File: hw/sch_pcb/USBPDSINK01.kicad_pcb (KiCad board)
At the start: 2 copper layers, 40.1 x 50.3 mm, 51 parts, among them J1 USBC_USB4105-GF-A, J2 HEADER_2x05_PARALLEL, J3 HEADER_2x04_PARALLEL, J4 HEADER_2x03_PARALLEL, J5 HEADER_2x01, J6 HEADER_2x07_PARALLEL, M1 HOLE, M2 HOLE, M3 HOLE, M4 HOLE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

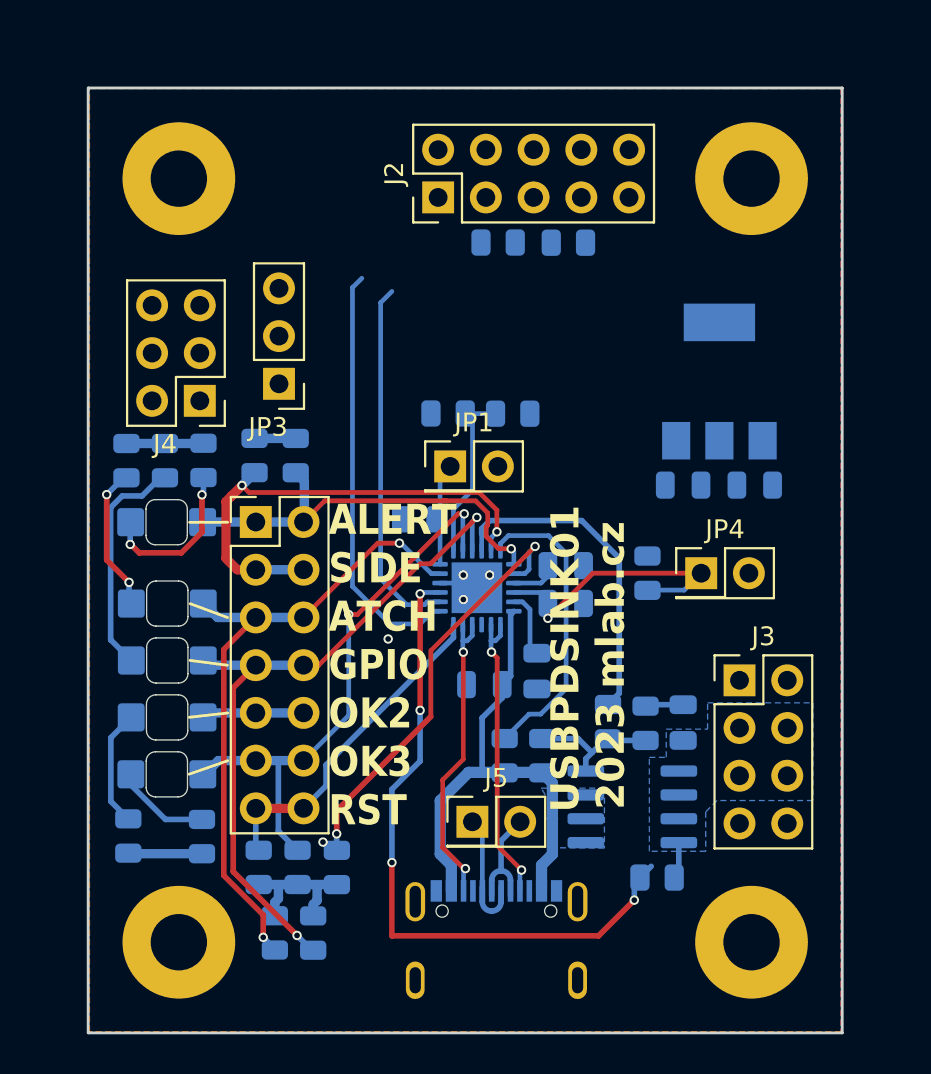
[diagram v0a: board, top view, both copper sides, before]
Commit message: update improvements in schematics and layout
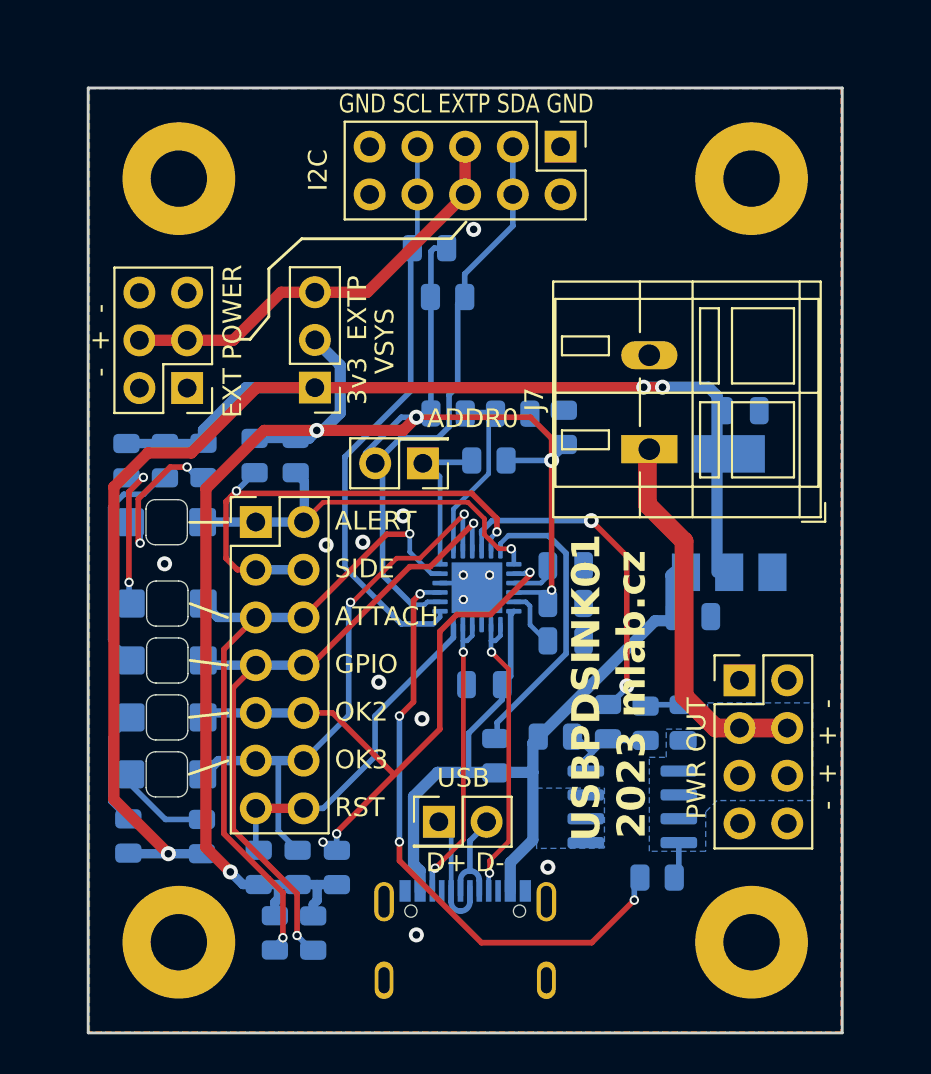
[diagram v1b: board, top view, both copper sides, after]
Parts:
- removed JP4: Jumper_2_Open, Connector_PinHeader_2.54mm:PinHeader_2x01_P2.54mm_Vertical
- added J7: WAGO, TerminalBlock_WAGO:TerminalBlock_WAGO_236-102_1x02_P5.00mm_45Degree, F.Cu at (158.3, 99.1)
- moved R22 8.95 mm to (153.8, 97.9)
- moved R14 7.40 mm to (146.6, 88.4), turned to 180 degrees
- moved J2 7.05 mm to (153.6, 83.0), turned to -90 degrees
- moved C6 7.02 mm to (160.6, 108.0)
- moved U2 7.02 mm to (162.6, 102.5)
- moved R1 4.87 mm to (149.8, 99.7), turned to 180 degrees
- moved C5 4.02 mm to (163.2, 97.0)
- moved R13 3.96 mm to (147.6, 91.0), turned to 0 degrees
- moved C1 2.22 mm to (153.8, 109.3), turned to 0 degrees
- moved JP3 1.92 mm to (140.5, 95.8)
- moved J5 1.78 mm to (147.1, 118.9)
- moved J1 1.66 mm to (148.5, 127.3)
- moved JP1 1.46 mm to (146.2, 99.8), turned to 180 degrees
- moved R10 1.23 mm to (153.3, 114.4), turned to 0 degrees
- moved J4 0.96 mm to (133.7, 95.8)
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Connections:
- net /VBUS renamed VBUS
- net /VOUT renamed VDC
- C7 pad 1: /VSYS -> VCC
- J2 pad 5: GND -> /EXT_PWR
- J2 pad 6: GND -> /EXT_PWR
- J4 pad 3: GND -> /EXT_PWR
- J4 pad 4: GND -> /EXT_PWR
- JP3 pad 3: GND -> /EXT_PWR
- R22 pad 2: /VSYS -> VCC
- U1 pad 22: /VSYS -> VCC
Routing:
- net VCC: track 9.85 -> 88.4 mm, vias 0 -> 5
- net +3V3: track 8.04 -> 81.2 mm, vias 0 -> 3
- net /EXT_PWR: track 0.00 -> 23.1 mm
- net VDC: track 1.96 -> 22.1 mm
- net VBUS: track 27.1 -> 42.7 mm
- net /VSYS: track 15.0 -> 0.00 mm, vias 1 -> 0
- net /SDA: track 19.3 -> 30.6 mm
- net /SCL: track 22.4 -> 30.8 mm
- net /PWR_OK2: track 29.2 -> 33.6 mm
- net /ADDR0: track 4.67 -> 8.45 mm
- net /DISCH: track 35.8 -> 32.3 mm
- net Net-(Q2-G): track 7.20 -> 5.30 mm
- net /ATTACH: track 34.7 -> 36.1 mm
- net Net-(D1-A): track 8.60 -> 7.41 mm
- net /ADDR1: track 8.95 -> 9.73 mm
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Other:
- board text added: "- + + -"
- board text added: "- + -"
- board text added: "3v3 EXTP"
- board text added: "ADDR 1"
- board text added: "ADDR0"
- board text added: "ALERT"
- board text added: "ATTACH"
- board text added: "D+ D-"
- board text added: "EXT POWER"
- board text added: "GND SCL EXTP SDA GND"
- board text added: "GPIO"
- board text added: "I2C"
- board text added: "OK2"
- board text added: "OK3"
- board text added: "PWR OUT"
- board text added: "RST"
- board text added: "SIDE"
- board text added: "USB"
- board text added: "VSYS"
- board text removed: "ALERT SIDE ATCH GPIO OK2 OK3 RST"

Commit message: solve DRC
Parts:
- moved C8 1.17 mm to (148.3, 111.6)
- moved R1 0.48 mm to (149.8, 99.2)
- moved R9 0.39 mm to (150.4, 115.1)
- moved C2 0.28 mm to (153.8, 105.0)
- moved J7 0.20 mm to (158.3, 98.9)
- moved C1 0.12 mm to (153.8, 109.4)
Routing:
- net VCC: track 88.4 -> 85.6 mm
- net +3V3: track 81.2 -> 80.1 mm
- net /PWR_OK2: track 33.6 -> 32.5 mm, vias 3 -> 2
- net /EXT_PWR: track 23.1 -> 23.9 mm
- net Net-(U1-VREG_1V2): track 1.95 -> 2.60 mm
- net /PWR_OK3: track 30.3 -> 30.8 mm
- net GND: track 2.17 -> 1.81 mm, vias 12 -> 13
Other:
- board text added: "+ -"
- board text added: "EXT POWER 3-5.5 V"
- board text added: "MLAB.cz 2023"
- board text added: "USB-C PD INPUT"
- board text added: "USBPDSINK01A"
- board text added: "USBPDSINK01A 2023 mlab.cz"
- board text removed: "EXT POWER"
- board text removed: "USBPDSINK01 2023 mlab.cz"

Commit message: silkscreen
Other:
- board text added: "CONNECTED"
- board text added: "ORIENTATION"
- board text removed: "ATTACH"
- board text removed: "SIDE"
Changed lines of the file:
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@@
     (48 "B.Fab" user)
     (49 "F.Fab" user)
-    (50 "User.1" user)
-    (51 "User.2" user)
-    (52 "User.3" user)
-    (53 "User.4" user)
-    (54 "User.5" user)
-    (55 "User.6" user)
-    (56 "User.7" user)
-    (57 "User.8" user)
-    (58 "User.9" user)
   )
   (setup
+    (stackup
+      (layer "F.SilkS" (type "Top Silk Screen") (color "Black"))
+      (layer "F.Paste" (type "Top Solder Paste"))
+      (layer "F.Mask" (type "Top Solder Mask") (color "White") (thickness 0.01))
+      (layer "F.Cu" (type "copper") (thickness 0.035))
+      (layer "dielectric 1" (type "core") (color "FR4 natural") (thickness 1.51) (material "FR4") (epsilon_r 4.5) (loss_tangent 0.02))
+      (layer "B.Cu" (type "copper") (thickness 0.035))
+      (layer "B.Mask" (type "Bottom Solder Mask") (color "Green") (thickness 0.01))
+      (layer "B.Paste" (type "Bottom Solder Paste"))
+      (layer "B.SilkS" (type "Bottom Silk Screen") (color "Black"))
+      (copper_finish "None")
+      (dielectric_constraints no)
+    )
     (pad_to_mask_clearance 0)
     (aux_axis_origin 123.1 135.48)
@@
     (effects (font (size 1 1) (thickness 0.15)) (justify left bottom mirror))
   )
-  (gr_text "ATTACH\n" (at 141.55 107.98) (layer "F.SilkS")
+  (gr_text "CONNECTED" (at 141.55 107.98) (layer "F.SilkS")
     (effects (font (size 1 1) (thickness 0.15)) (justify left))
   )
@@
     (effects (font (size 1.5 1.5) (thickness 0.3) bold))
   )
-  (gr_text "SIDE" (at 141.55 105.438334) (layer "F.SilkS")
+  (gr_text "ORIENTATION" (at 141.55 105.438334) (layer "F.SilkS")
     (effects (font (size 1 1) (thickness 0.15)) (justify left))
   )
@@
         (xy 167 112.58)
         (xy 167 117.78)
-        (xy 161.9 117.78)
-        (xy 161.3 118.38)
+        (xy 161.9 117.68)
+        (xy 161.3 118.28)
         (xy 161.3 120.48)
         (xy 158.3 120.48)

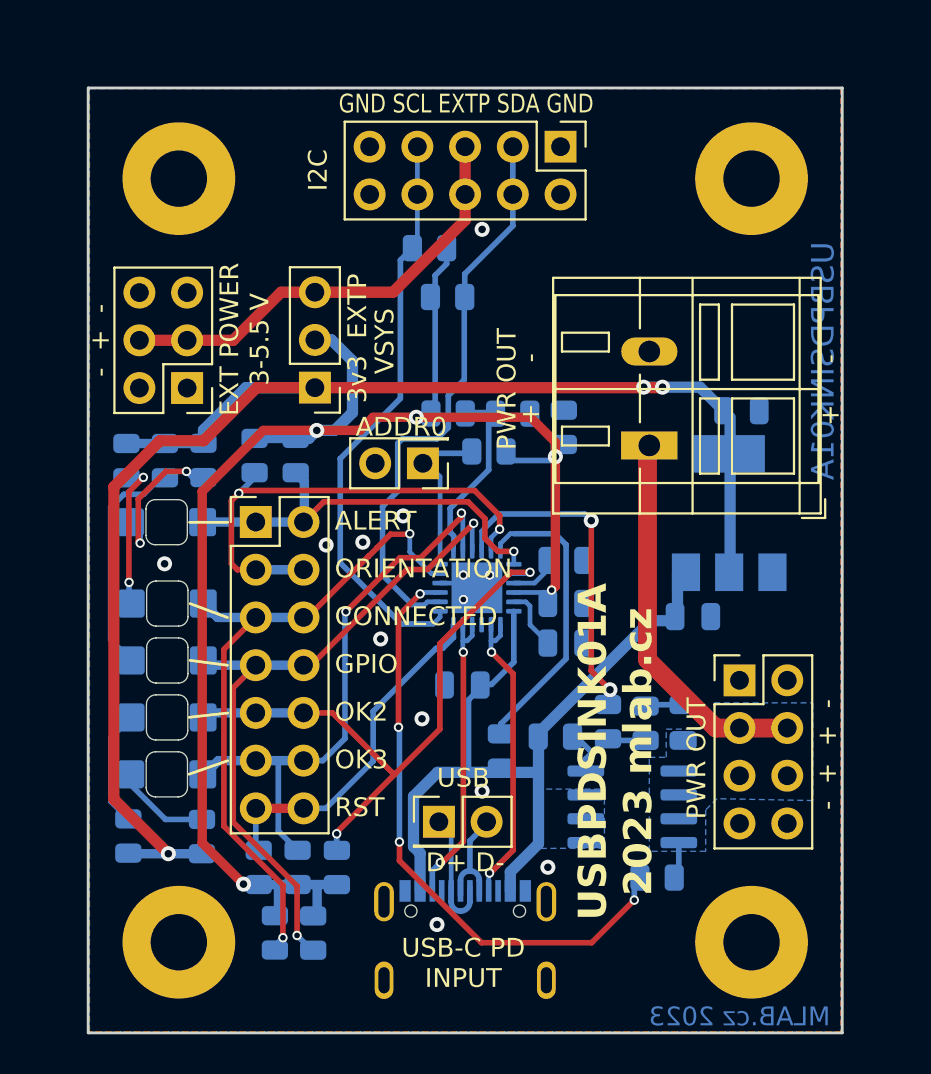
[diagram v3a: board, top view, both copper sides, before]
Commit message: update wago connector
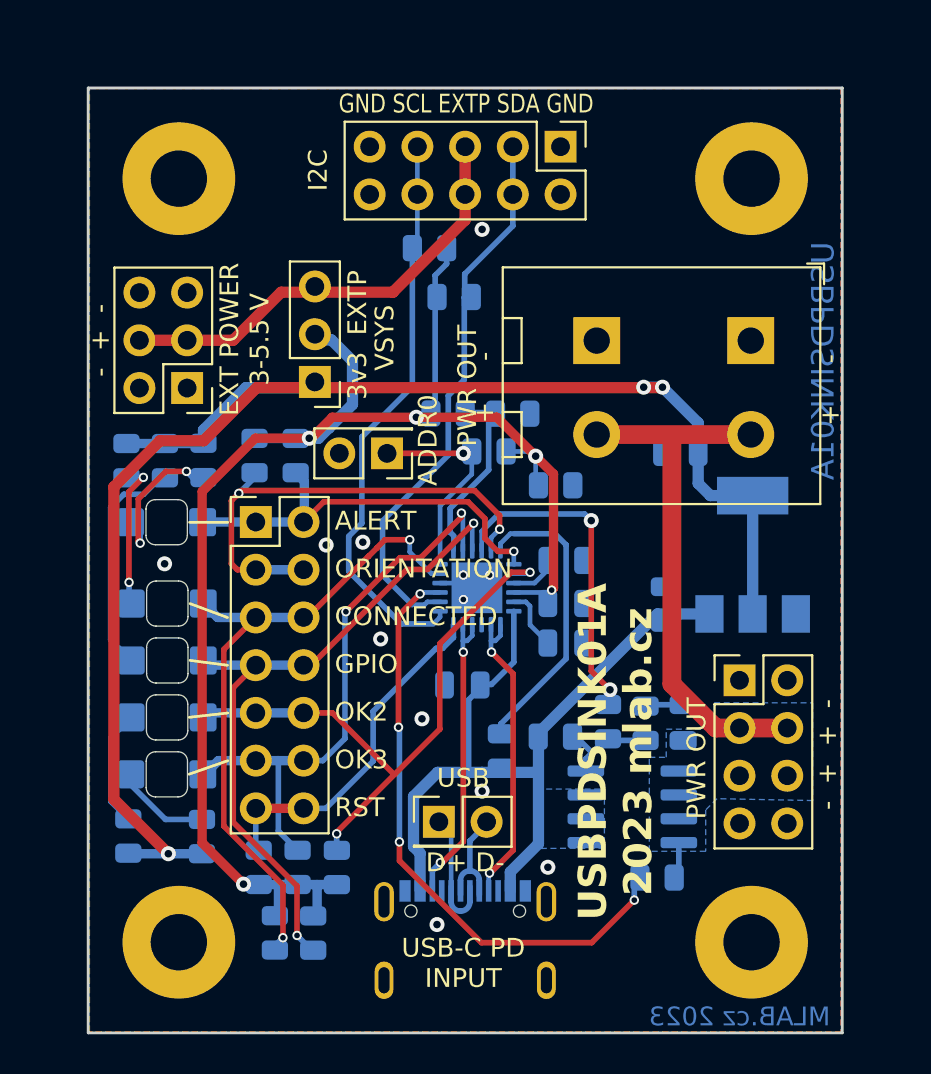
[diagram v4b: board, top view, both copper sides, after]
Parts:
- D1, D4: value LED -> RED
- D2: value LED -> YELLOW
- D3: value LED -> ORANGE
- D5: value LED -> GREEN
- J7: value WAGO -> WAGO_2604-3102; footprint TerminalBlock_WAGO:TerminalBlock_WAGO_236-102_1x02_P5.00mm_45Degree -> Mlab_CON:TerminalBlock_WAGO_2604-3102_1x02_P5.00mm_Vertical
- R13, R14, R15, R16, R17, R18, R19, R20, R21: value R -> 4k7
- moved J7 7.77 mm to (163.7, 93.3), turned to -90 degrees
- moved C5 3.94 mm to (159.9, 99.2), turned to 180 degrees
- moved R22 3.11 mm to (153.3, 101.0), turned to 180 degrees
- moved U2 2.55 mm to (163.8, 104.7)
- moved JP1 1.98 mm to (144.3, 99.3)
- moved C6 1.65 mm to (159.1, 107.3), turned to 90 degrees
- moved R13 0.35 mm to (147.9, 91.0)
- moved JP3 0.31 mm to (140.5, 95.5)
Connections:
- J7 pad 1: VDC -> GND
- J7 pad 2: GND -> VDC
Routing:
- net VDC: track 22.1 -> 30.5 mm
- net +3V3: track 80.1 -> 85.4 mm
- net /ADDR0: track 8.45 -> 11.3 mm, vias 0 -> 1
- net VCC: track 85.6 -> 84.1 mm
- net /SDA: track 30.5 -> 29.4 mm
- net VBUS: track 43.2 -> 42.6 mm
- net GND: track 1.81 -> 1.71 mm, vias 13 -> 12

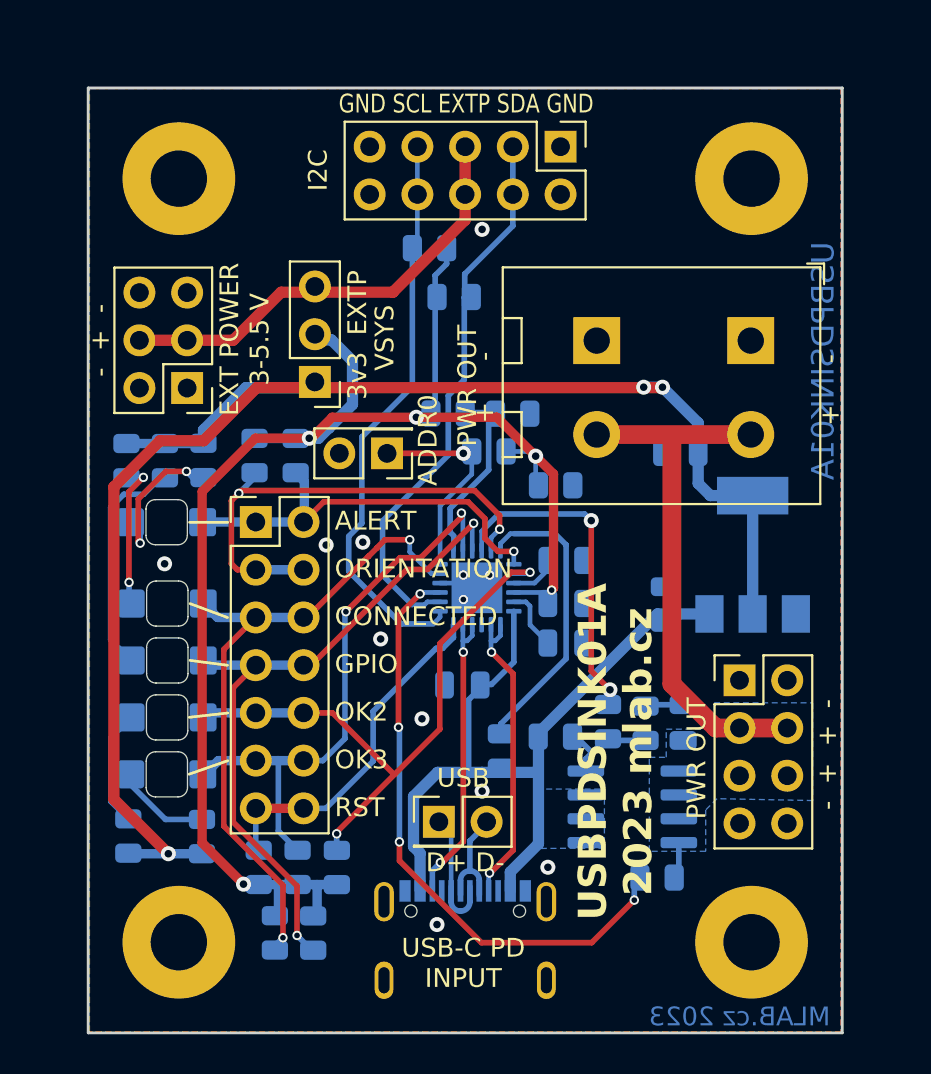
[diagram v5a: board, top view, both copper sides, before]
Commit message: minor updates in layout, clean schematics, add components MFPN
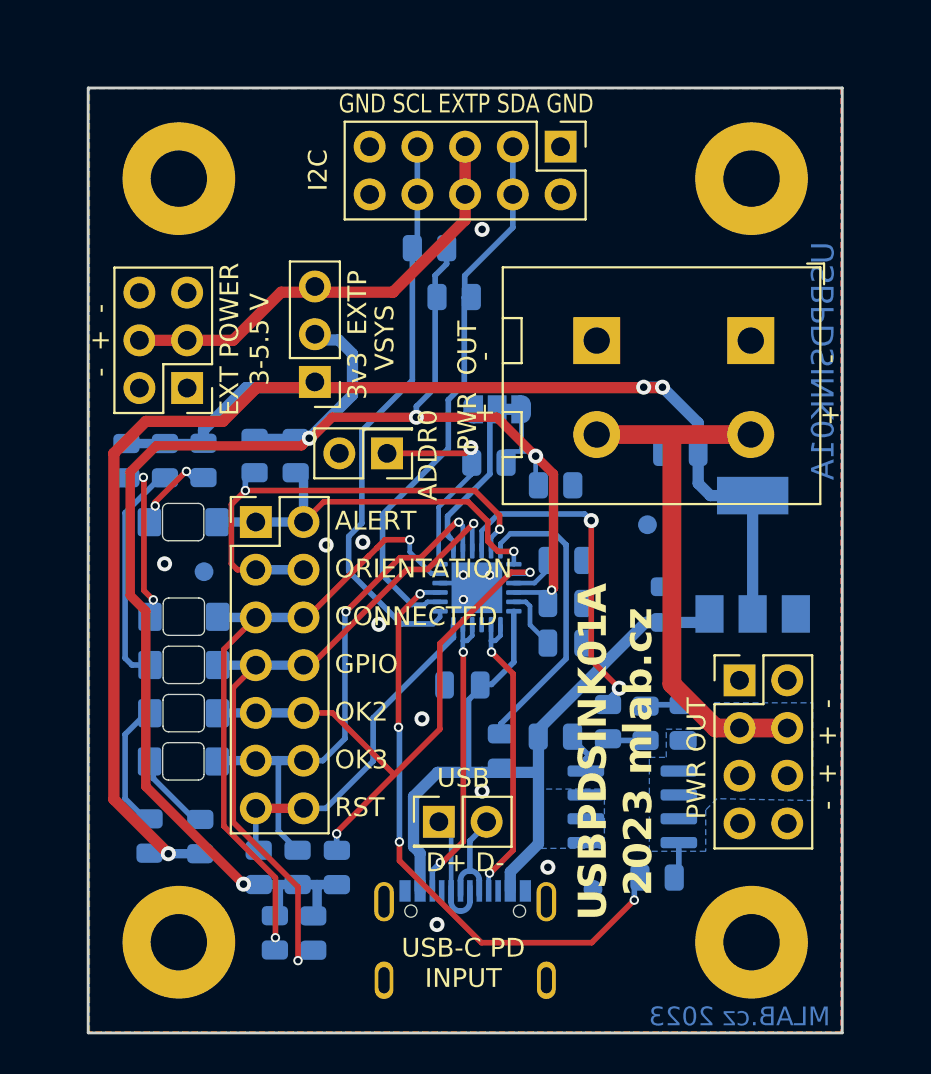
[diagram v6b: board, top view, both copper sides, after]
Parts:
- removed R2: 100k, Resistor_SMD:R_0805_2012Metric
- removed R23: 100K, Resistor_SMD:R_0805_2012Metric
- added FID1: Fiducial, Fiducial:Fiducial_1mm_Mask2mm, B.Cu at (134.6, 105.6)
- added FID2: Fiducial, Fiducial:Fiducial_1mm_Mask2mm, B.Cu at (155.3, 122.5)
- added FID3: Fiducial, Fiducial:Fiducial_1mm_Mask2mm, B.Cu at (158.2, 103.1)
- added JP2: Jumper_3_Bridged12, Jumper:SolderJumper-3_P1.3mm_Bridged12_RoundedPad1.0x1.5mm, B.Cu at (150.2, 97.0)
- D1, D2, D4, D5: footprint Mlab_D:LED_1206_2 -> Mlab_D:LED_1206_mill
- D3: value ORANGE -> BLUE; footprint Mlab_D:LED_1206_2 -> Mlab_D:LED_1206_mill
- Q2: value IRF7469PbF -> IRF9317TRPBF
- R10, R22: value 100K -> 100k
- R3, R5, R6: value R -> 65R
- R4: value R -> R10
- R7: value R -> 60R
- moved R4 1.13 mm to (131.7, 119.7)
- moved D5 1.13 mm to (133.5, 108.0)
- moved D4 1.12 mm to (133.5, 115.7)
- moved D2 0.91 mm to (133.5, 110.6)
- moved D3 0.91 mm to (133.5, 113.1)
- moved D1 0.88 mm to (133.5, 103.0)
- moved R1 0.60 mm to (149.8, 99.8)
- moved R3 0.09 mm to (134.4, 119.7)
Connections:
- J2 pad 5: /EXT_PWR -> GND
- J2 pad 6: /EXT_PWR -> GND
- J4 pad 3: /EXT_PWR -> GND
- J4 pad 4: /EXT_PWR -> GND
- JP3 pad 3: /EXT_PWR -> GND
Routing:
- net GND: track 1.71 -> 25.6 mm
- net /EXT_PWR: track 23.9 -> 0.00 mm
- net VCC: track 84.1 -> 91.6 mm
- net Net-(D1-A): track 7.22 -> 3.58 mm
- net /PWR_OK3: track 30.8 -> 29.1 mm
- net /ALERT: track 22.2 -> 21.0 mm
- net /ATTACH: track 35.6 -> 34.4 mm
- net /ADDR1: track 9.90 -> 8.76 mm
- net Net-(D4-A): track 5.11 -> 4.19 mm
- net /SIDE: track 25.9 -> 25.0 mm
- net /PWR_OK2: track 32.5 -> 31.6 mm
- net VBUS: track 42.6 -> 42.1 mm
- net Net-(D3-A): track 6.23 -> 6.76 mm

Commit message: version uploaded to aisler
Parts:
- moved J2 0.12 mm to (153.6, 83.1)
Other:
- board size 40.1 x 50.3 mm -> 45.5 x 52.9 mm
